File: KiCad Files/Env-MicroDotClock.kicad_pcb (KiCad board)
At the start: 2 copper layers, 90 x 65.2 mm, 47 parts, among them IC1 IS31FL3730-QFLS2-TR, IC2 IS31FL3730-QFLS2-TR, IC3 IS31FL3730-QFLS2-TR, IC4 IS31FL3730-QFLS2-TR, M1 Dip-14 Socket, M2 Dip-14 Socket, M3 Dip-14 Socket, M4 Dip-14 Socket, M5 Dip-14 Socket, M6 Dip-14 Socket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

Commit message: Added Signatures
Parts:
- added G***: LOGO, LOGO, F.Cu at (125.6, 119.8)

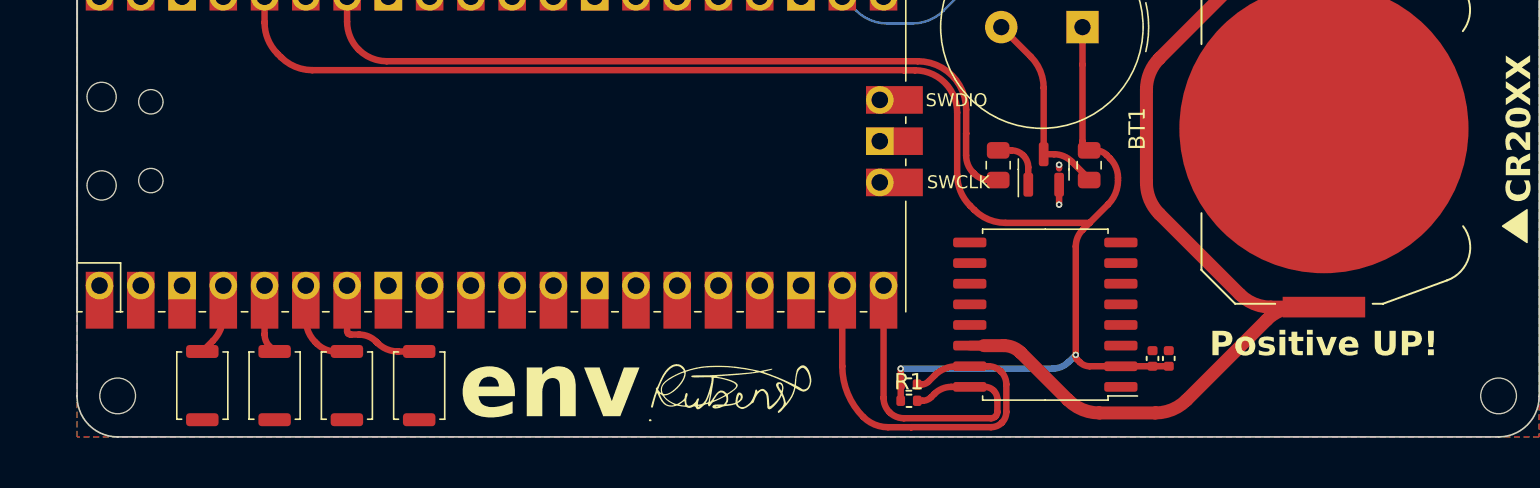
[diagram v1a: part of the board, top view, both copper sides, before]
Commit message: Added debugging headder and sig
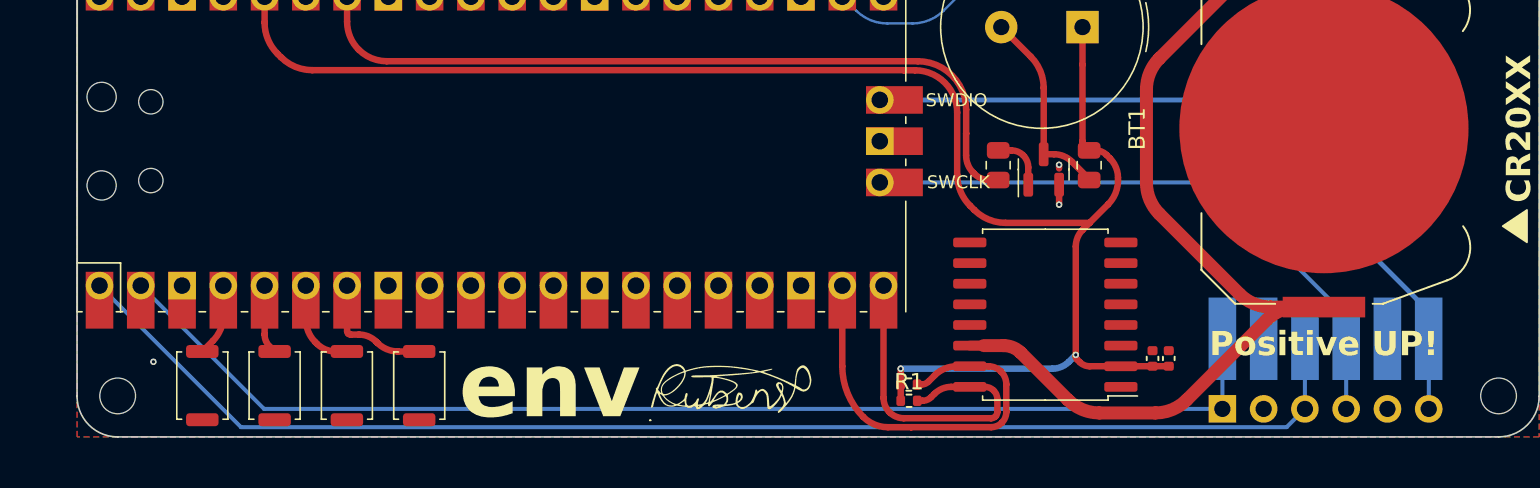
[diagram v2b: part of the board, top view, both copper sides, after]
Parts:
- added J1: Conn_01x06_Pin, Connector_PinHeader_2.54mm:PinHeader_1x06_P2.54mm_Vertical, B.Cu at (155.5, 121.0)
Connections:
- U1 pad 1: unconnected-(U1-GPIO0-Pad1) -> TX
- U1 pad 2: unconnected-(U1-GPIO1-Pad2) -> RX
- U1 pad 41: unconnected-(U1-SWCLK-Pad41) -> SWCLK
- U1 pad 42: unconnected-(U1-GND-Pad42) -> GND
- U1 pad 43: unconnected-(U1-SWDIO-Pad43) -> SWDIO
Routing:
- net TX: track 0.00 -> 82.6 mm
- net RX: track 0.00 -> 74.0 mm
- net SWDIO: track 0.00 -> 45.2 mm
- net SWCLK: track 0.00 -> 39.5 mm
- net GND: vias 44 -> 45

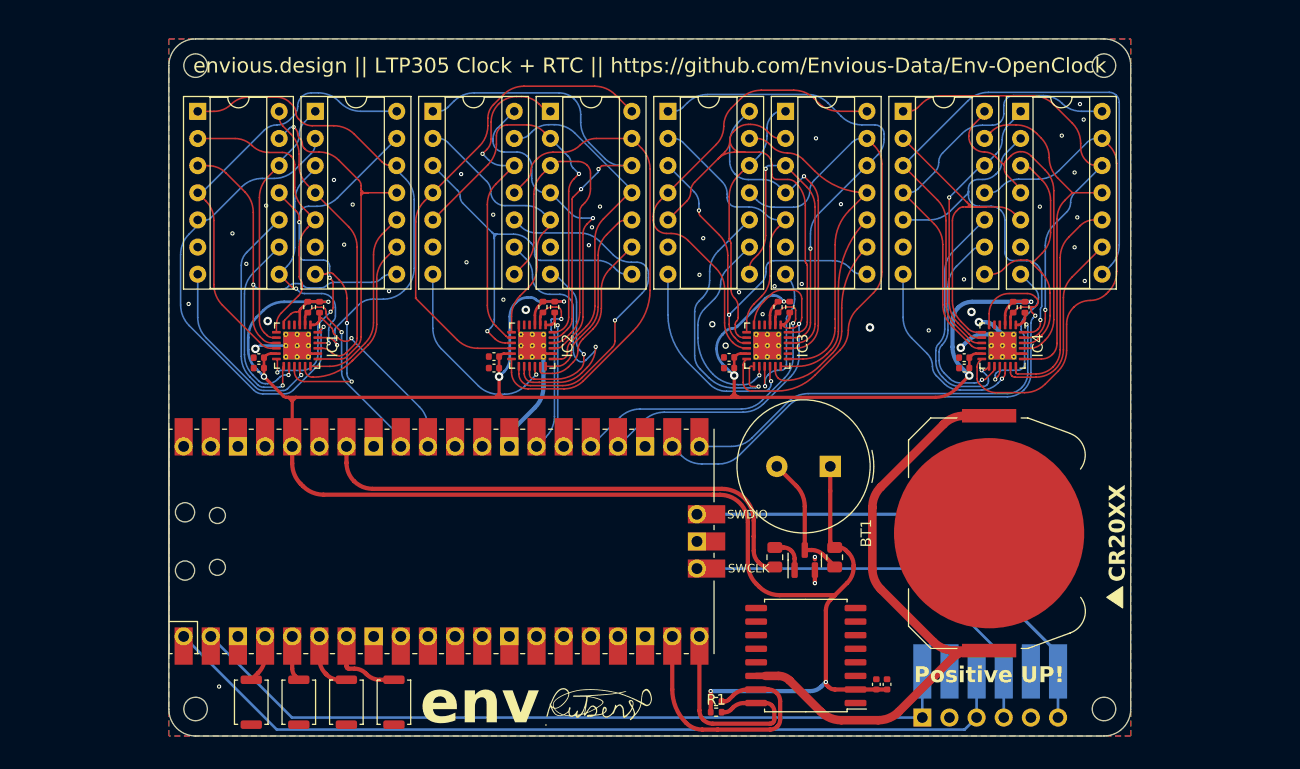
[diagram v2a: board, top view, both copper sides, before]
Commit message: prettied up pcb some more and organised schematic
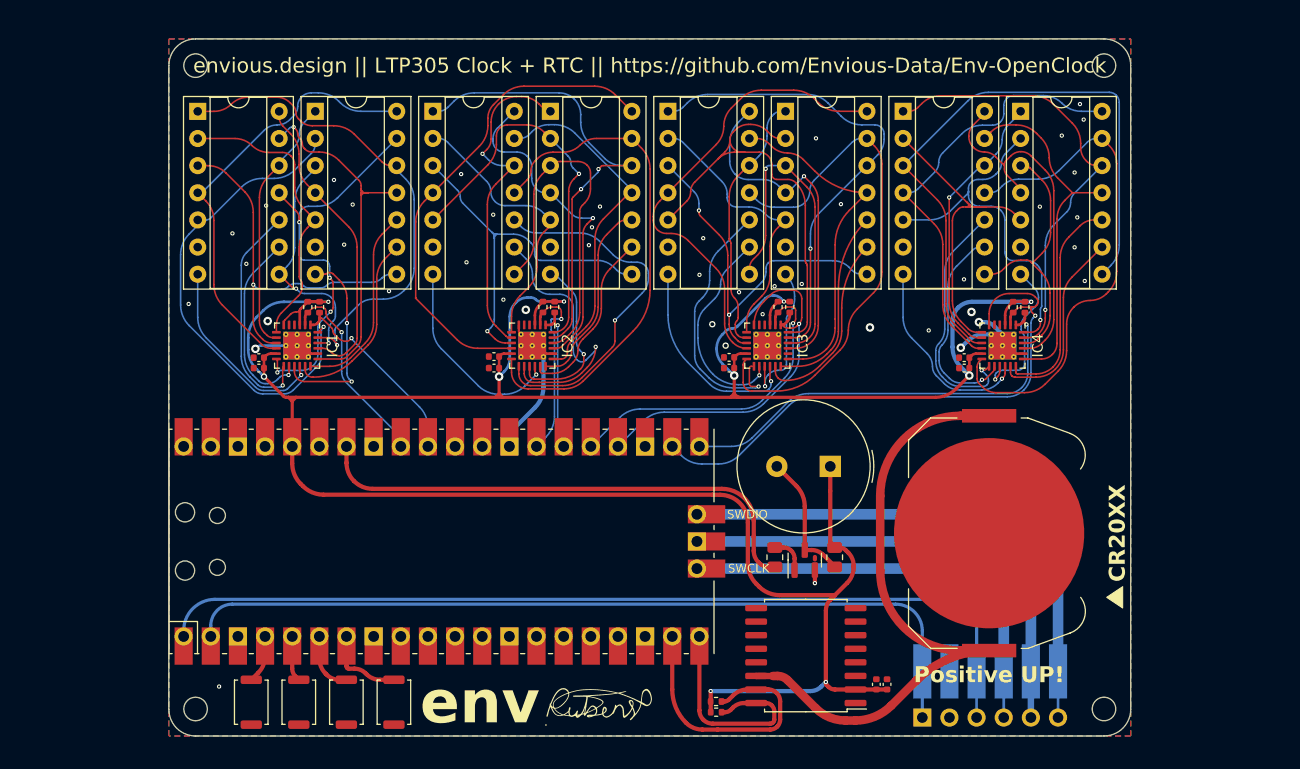
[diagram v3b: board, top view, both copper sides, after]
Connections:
- J1 pad 5: GND -> DEBUG-GND
- U1 pad 42: GND -> DEBUG-GND
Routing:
- net DEBUG-GND: track 0.00 -> 46.6 mm
- net SWDIO: track 45.2 -> 51.6 mm
- net RX: track 74.0 -> 78.1 mm
- net TX: track 82.6 -> 86.2 mm
- net SWCLK: track 39.5 -> 41.5 mm
- net GND: track 33.6 -> 34.7 mm, vias 45 -> 44
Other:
- board text added: "RX GND TX SWCLK GND SWDIO"

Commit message: added more buttons, re-worked some bits and pieces here and there.
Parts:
- added SW5: SW_SPST, Button_Switch_SMD:SW_Push_SPST_NO_Alps_SKRK, F.Cu at (120.4, 119.9)
- added SW6: SW_SPST, Button_Switch_SMD:SW_Push_SPST_NO_Alps_SKRK, F.Cu at (127.3, 119.9)
- SW1, SW2, SW3, SW4: value SKRK -> SW_SPST
- moved G*** 71.6 mm to (165.1, 60.0)
- moved SW4 7.42 mm to (113.5, 119.9), turned to -45 degrees
- moved SW3 4.96 mm to (106.6, 119.9), turned to -45 degrees
- moved SW2 2.50 mm to (99.6, 119.9), turned to -45 degrees
- moved SW1 0.35 mm to (92.7, 119.9), turned to -45 degrees
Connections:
- U1 pad 10: unconnected-(U1-GPIO7-Pad10) -> GPIO7
- U1 pad 11: unconnected-(U1-GPIO8-Pad11) -> GPIO9
- U1 pad 12: unconnected-(U1-GPIO9-Pad12) -> GPIO8
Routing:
- net GPIO7: track 0.00 -> 21.0 mm
- net GPIO6: track 0.00 -> 15.5 mm
- net GPIO5: track 7.63 -> 14.6 mm
- net GPIO4: track 5.73 -> 9.87 mm
- net GPIO2: track 4.48 -> 5.91 mm
- net GPIO3: track 4.26 -> 5.42 mm
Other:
- board text added: "CR2020 CR2025 CR2032"
- board text added: "https://GitHub.com/Envious-Data/Env-OpenClock"
- board text removed: "CR20XX"
- board text removed: "envious.design || LTP305 Clock + RTC || https://github.com/Envious-Data/Env-OpenClock"

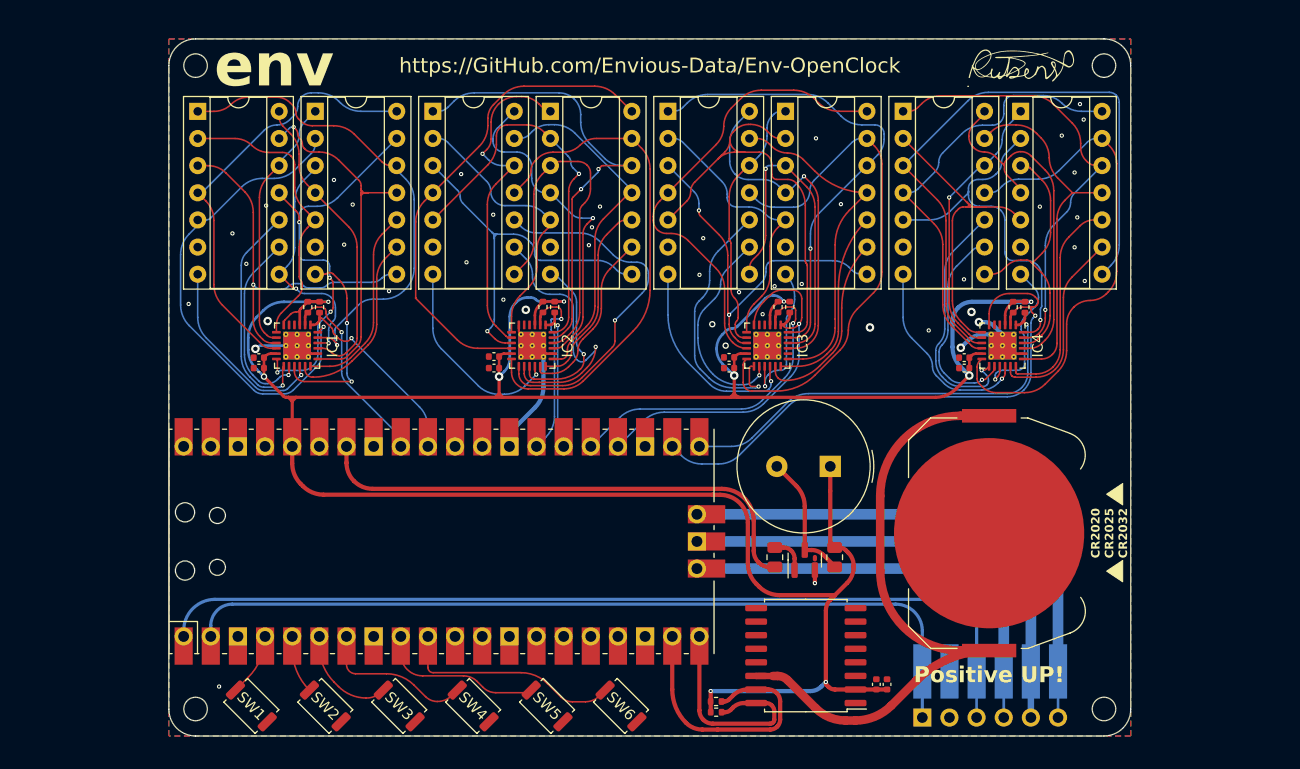
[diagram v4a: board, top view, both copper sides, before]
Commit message: added missing teardrops and fixed a couple overlapped traces
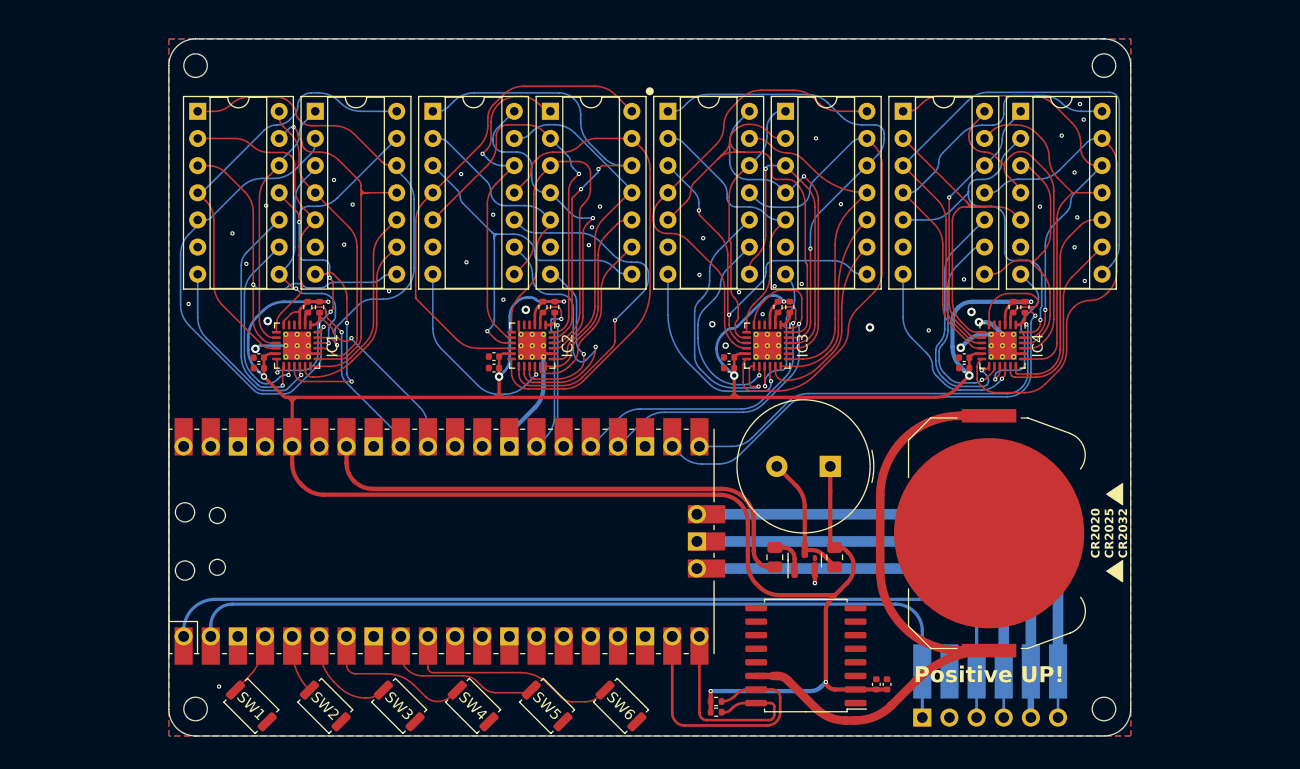
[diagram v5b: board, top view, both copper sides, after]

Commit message: Re-worked board to have optional VCC source, rear usb and a few other adjustments
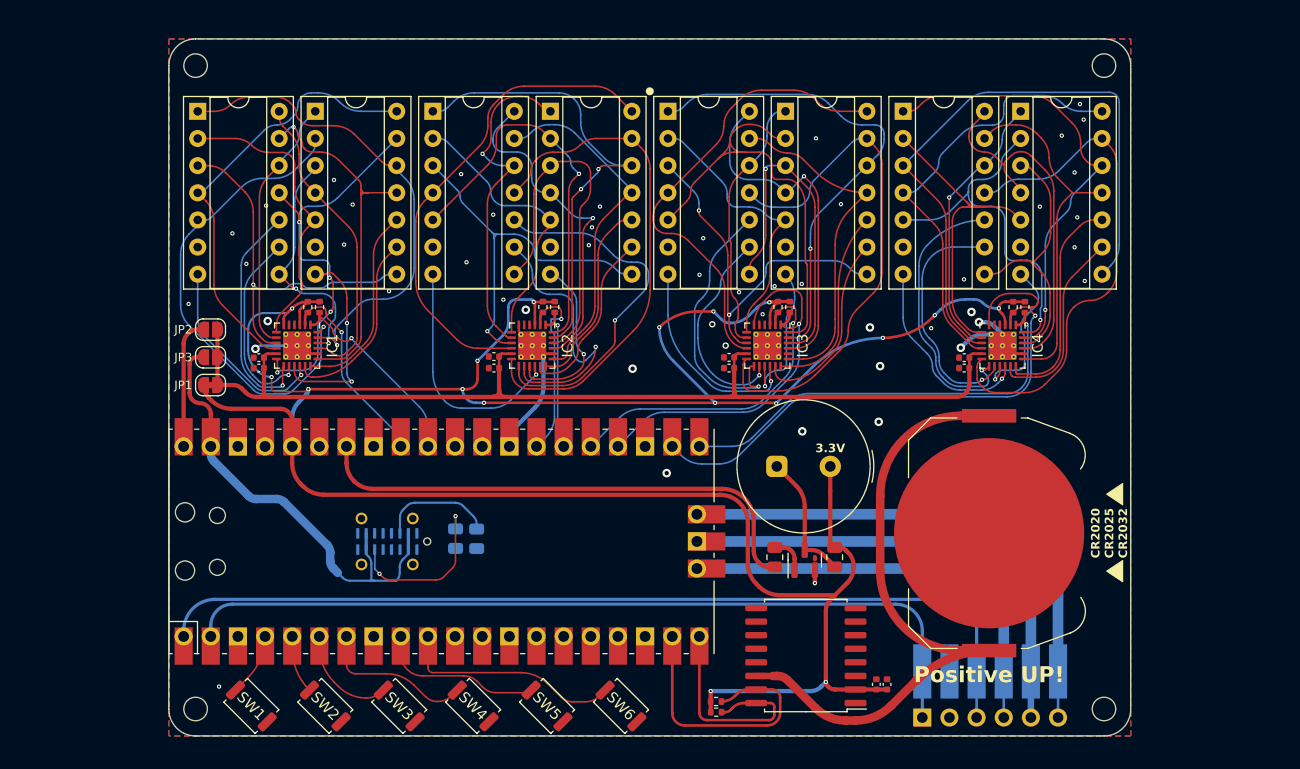
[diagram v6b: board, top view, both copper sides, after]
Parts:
- added J2: GT-USB-7051, Connector_USB:USB_C_Receptacle_G-Switch_GT-USB-7051x, B.Cu at (105.4, 104.5)
- added JP1: bridge, Jumper:SolderJumper-2_P1.3mm_Bridged_RoundedPad1.0x1.5mm, F.Cu at (88.9, 89.9)
- added JP2: bridge, Jumper:SolderJumper-2_P1.3mm_Open_RoundedPad1.0x1.5mm, F.Cu at (88.9, 84.7)
- added JP3: bridge, Jumper:SolderJumper-2_P1.3mm_Open_RoundedPad1.0x1.5mm, F.Cu at (88.9, 87.3)
- added R13: 5.1K 0805, Resistor_SMD:R_0805_2012Metric, B.Cu at (111.8, 104.3)
- added R14: 5.1K 0805, Resistor_SMD:R_0805_2012Metric, B.Cu at (113.8, 104.3)
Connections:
- C1 pad 1: +3V3 -> VCC
- C2 pad 1: +3V3 -> VCC
- C3 pad 1: +3V3 -> VCC
- C4 pad 1: +3V3 -> VCC
- C5 pad 1: +3V3 -> VCC
- C6 pad 1: +3V3 -> VCC
- C7 pad 1: +3V3 -> VCC
- C8 pad 1: +3V3 -> VCC
- IC1 pad 11: +3V3 -> VCC
- IC2 pad 11: +3V3 -> VCC
- IC3 pad 11: +3V3 -> VCC
- IC4 pad 11: +3V3 -> VCC
- U1 pad 39: unconnected-(U1-VSYS-Pad39) -> VDD
- U1 pad 40: unconnected-(U1-VBUS-Pad40) -> VBUS
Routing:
- net VCC: track 0.00 -> 100.6 mm
- net VDD: track 0.00 -> 44.3 mm
- net Net-(J2-CC2): track 0.00 -> 16.0 mm, vias 0 -> 2
- net VBUS: track 0.00 -> 12.2 mm
- net Net-(J2-CC1): track 0.00 -> 10.8 mm
- net +3V3: track 266.6 -> 260.2 mm, vias 10 -> 17
- net IC2C8: track 19.1 -> 22.9 mm
- net IC4R7: track 19.6 -> 22.6 mm
- net IC4R6: track 23.4 -> 26.1 mm
- net SWDIO: track 51.6 -> 50.5 mm
- net GND: vias 44 -> 49
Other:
- board text added: "3.3V"
